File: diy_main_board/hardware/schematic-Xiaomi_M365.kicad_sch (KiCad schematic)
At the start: 8 parts, among them J1 Connector_1, J2 Connector_2, U1 ESP32-S3-DevKitC

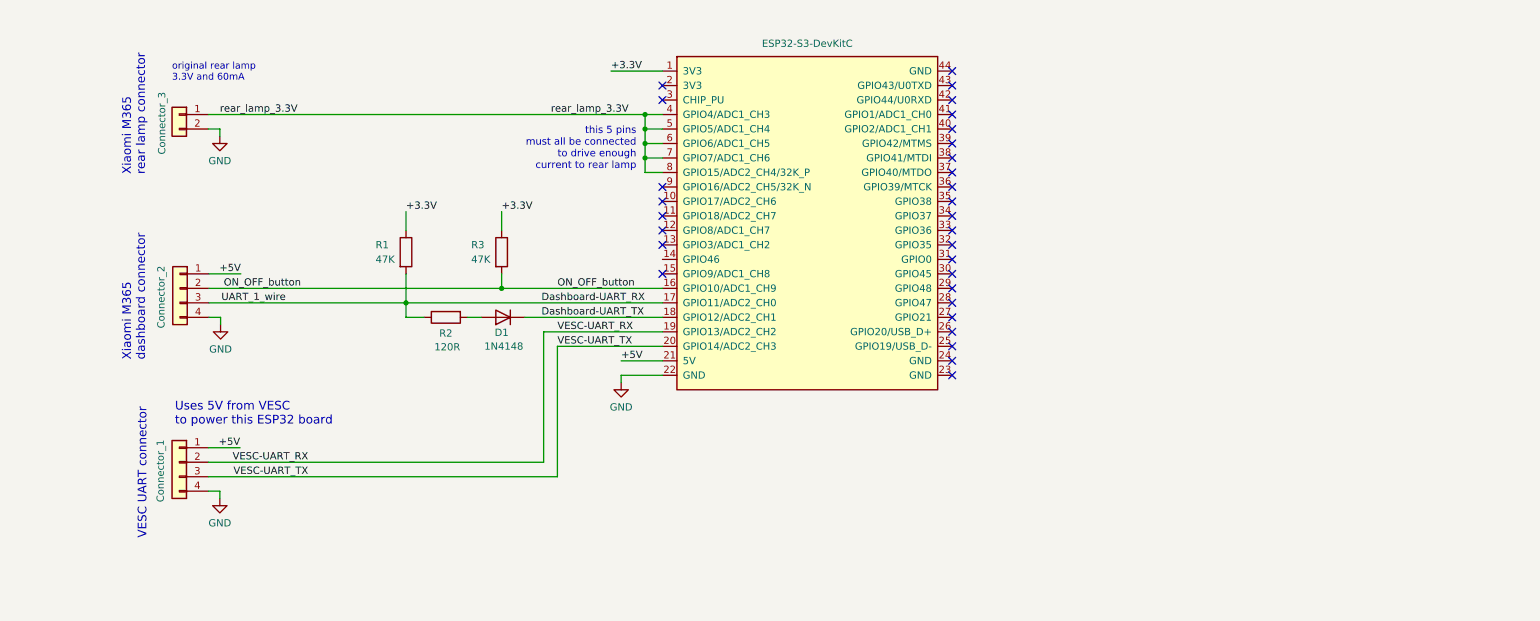
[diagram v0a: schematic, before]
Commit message: Changed motor main board to use ESP32-C3 instead of ESP32-S3
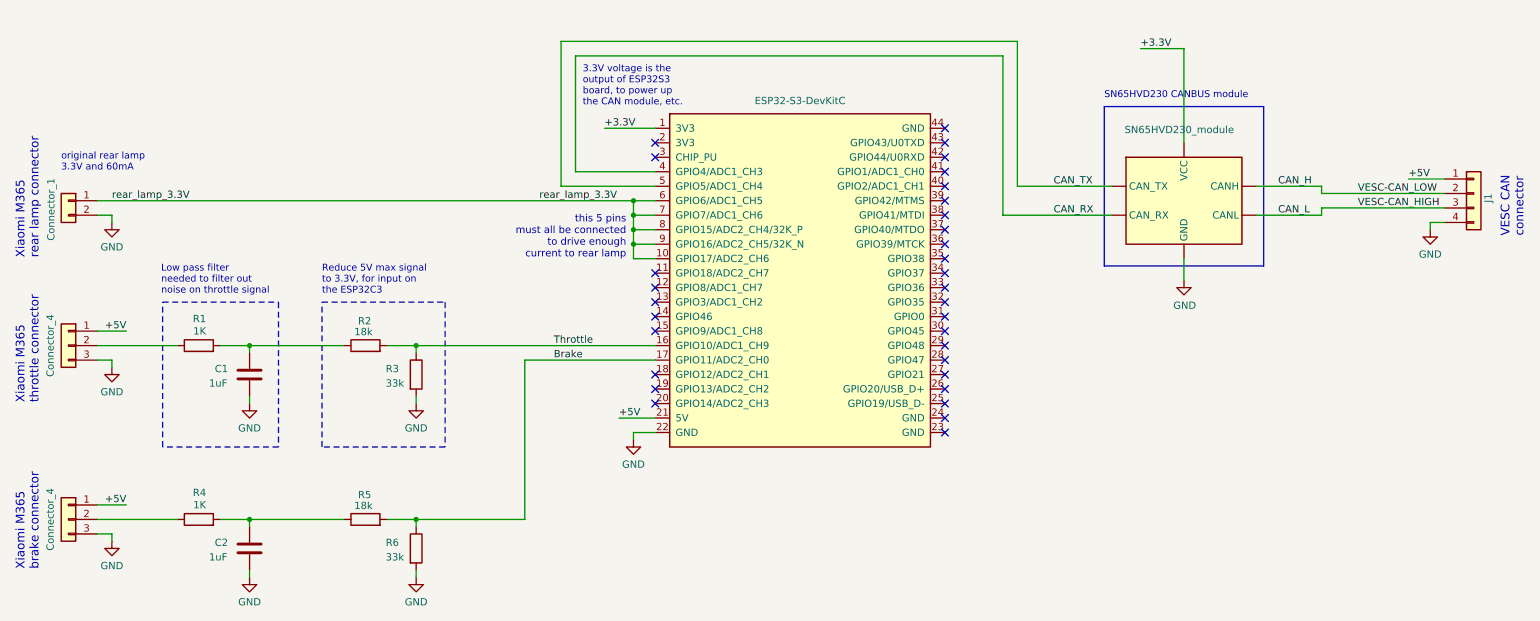
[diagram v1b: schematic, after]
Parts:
- removed Connector_3: ~, symbol Connector_Generic:Conn_01x02
- removed D1: 1N4148, Diode_THT:D_DO-35_SOD27_P7.62mm_Horizontal, symbol Diode:1N4148
- removed J2: Connector_2, symbol Connector_Generic:Conn_01x04
- removed U1: ESP32-S3-DevKitC, Espressif:ESP32-S3-DevKitC, symbol Espressif:ESP32-S3-DevKitC
- added C1, C2: 1uF, symbol Device:C
- added Connector_1: ~, symbol Connector_Generic:Conn_01x02
- added J2, J3: Connector_4, symbol Connector_Generic:Conn_01x03
- added R4: 1K, symbol Device:R
- added R5: 18k, symbol Device:R
- added R6: 33k, symbol Device:R
- added U1: SN65HVD230_module, symbol TJA1050:TJA1050_module
- added U2: ESP32-S3-DevKitC, Espressif:ESP32-S3-DevKitC, symbol Espressif:ESP32-S3-DevKitC
- J1: value Connector_1 -> Conn_01x04
- R1: value 47K -> 1K
- R2: value 120R -> 18k
- R3: value 47K -> 33k
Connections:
- net ON_OFF_button is gone; now on net GND: R3.2
- net +3.3V: now also U1. (VCC), U2.1 (3V3); no longer R1.1, R3.1
- net +5V: now also J2.1 (Pin_1), J3.1 (Pin_1), U2.21 (5V)
- net GND: now also C1.2, C2.2, Connector_1.2 (Pin_2), J2.3 (Pin_3), J3.3 (Pin_3), R6.2, U1. (VCC), U2.22 (GND)
- net rear_lamp_3.3V: now also Connector_1.1 (Pin_1), U2.10 (GPIO17/ADC2_CH6), U2.6 (GPIO6/ADC1_CH5), U2.7 (GPIO7/ADC1_CH6), U2.8 (GPIO15/ADC2_CH4/32K_P), U2.9 (GPIO16/ADC2_CH5/32K_N)
- net Throttle: now reaches R2.2
- net Throttle: now also R3.1, U2.16 (GPIO10/ADC1_CH9)
- net Dashboard-UART_RX: no longer names the net of R1.2, R2.1
- net Dashboard-UART_RX: now also C1.1
- net VESC-UART_RX renamed CAN_H
- net CAN_H: now also U1. (VCC)
- net VESC-UART_TX renamed CAN_L
- net CAN_L: now also U1. (VCC)
- new net: J3.2 (Pin_2), R4.1
- new net: C2.1, R4.2, R5.1
- new net: J2.2 (Pin_2), R1.1
- new net Brake: R5.2, R6.1, U2.17 (GPIO11/ADC2_CH0)
- new net CAN_RX: U1. (VCC), U2.4 (GPIO4/ADC1_CH3)
- new net CAN_TX: U1. (VCC), U2.5 (GPIO5/ADC1_CH4)
- no-connect marks 30 -> 32
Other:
- note added: "3.3V voltage is the output of ESP32S3 board, to power up the CAN module, etc."
- note added: "Low pass filter needed to filter out noise on throttle signal"
- note added: "Reduce 5V max signal to 3.3V, for input on the ESP32C3"
- note added: "SN65HVD230 CANBUS module"
- note added: "VESC CAN connector"
- note added: "Xiaomi M365 brake connector"
- note added: "Xiaomi M365 throttle connector"
- note removed: "Uses 5V from VESC to power this ESP32 board"
- note removed: "VESC UART connector"
- note removed: "Xiaomi M365 dashboard connector"
